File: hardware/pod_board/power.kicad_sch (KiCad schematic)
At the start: 11 parts, among them J2 12 V ACC in

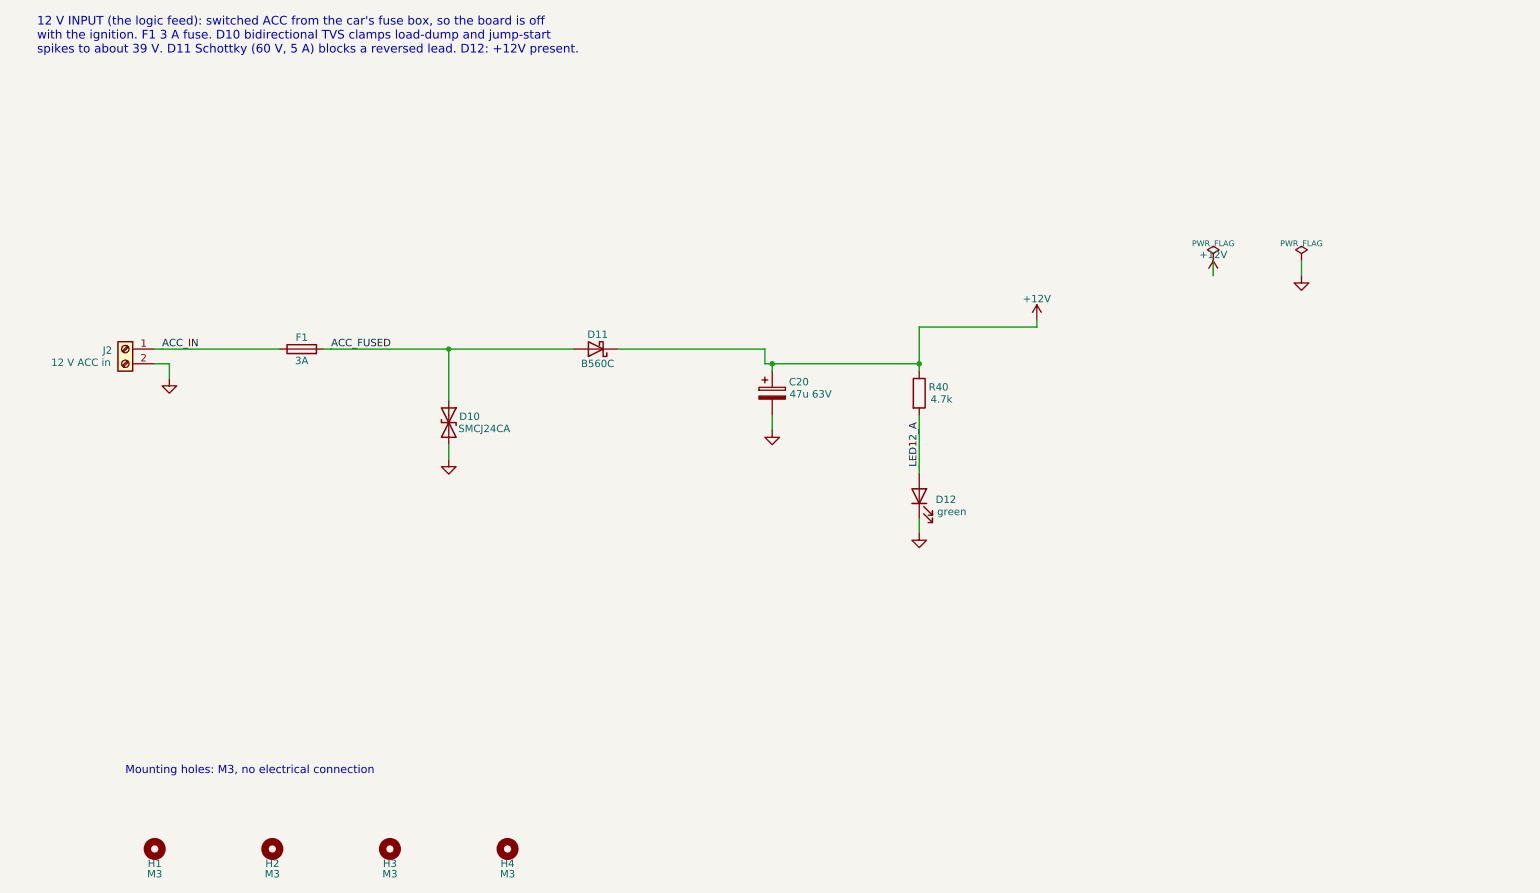
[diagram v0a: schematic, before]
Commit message: Pod board schematic redrawn as wired sheets; duplicate references fixed
pod_board_drawing.py draws six sheets around an MCU sheet under a block
diagram; check.sh now compares both boards' drawn and label-only netlists.
kisheet.py: stacked pins, PWR_FLAGs on signal nets, column hints for
crossing-free fan-ins, nets drawn in pieces joined by name, and visible
rail names on power symbols.

R31-R33 were used twice on the pod board, which KiCad's ERC does not
report; the netlist merged each pair. Cable parts now start at R40/C40,
generate.py rejects duplicate references and check_nets.py fails on a pin
in two nets. check_nets.py also drops the sheet path from net names.
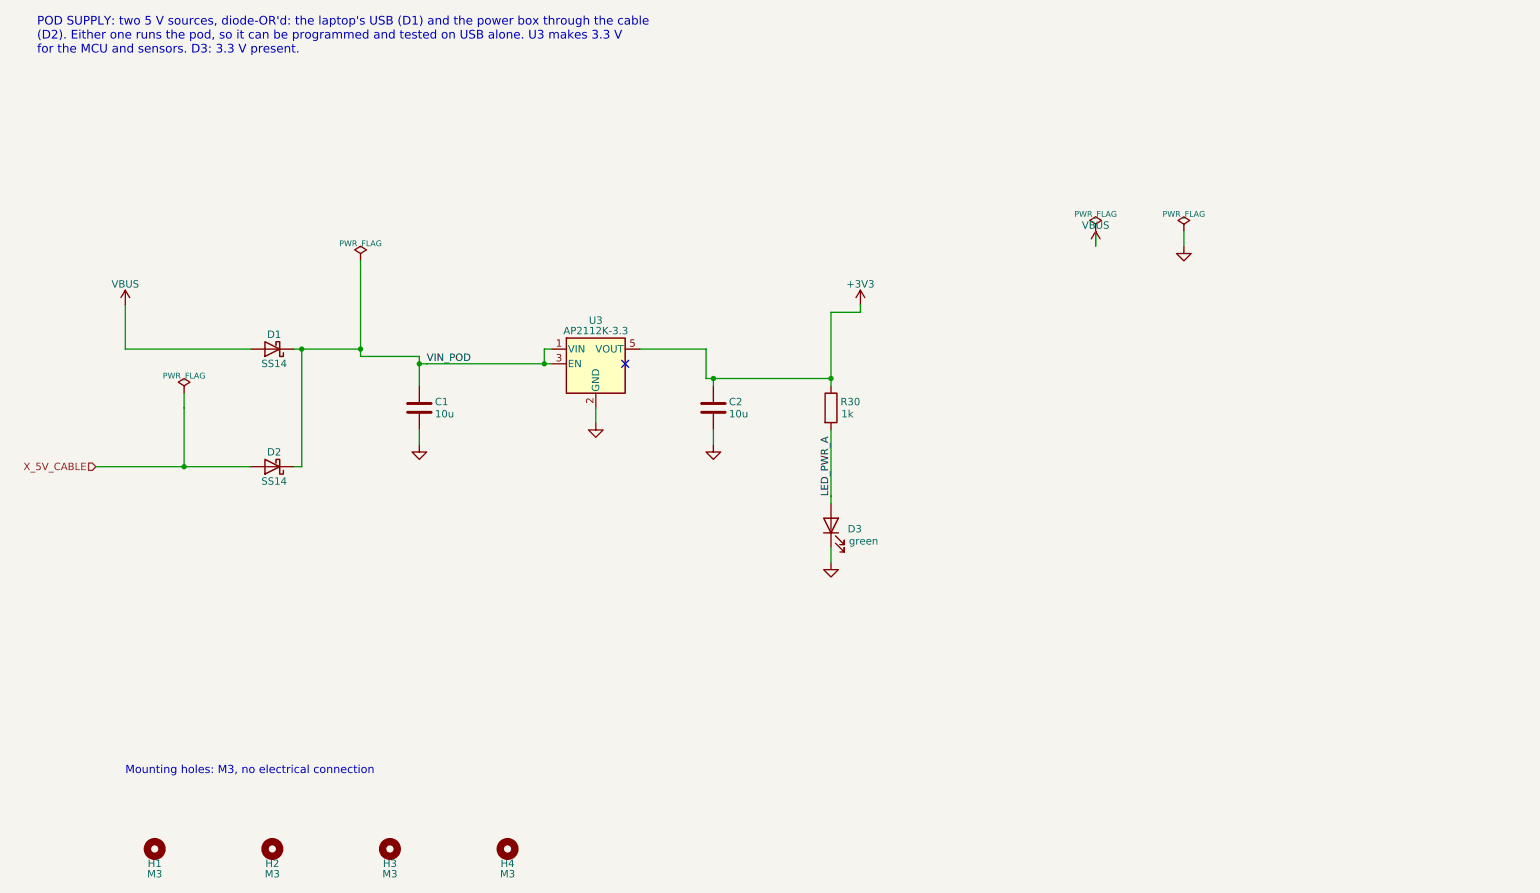
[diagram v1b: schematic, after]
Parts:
- removed C20: 47u 63V, Capacitor_THT:CP_Radial_D8.0mm_P3.50mm, symbol Device:C_Polarized
- removed D10: SMCJ24CA, Diode_SMD:D_SMC, symbol Device:D_TVS
- removed D11: B560C, Diode_SMD:D_SMC, symbol Device:D_Schottky
- removed D12: green, LED_SMD:LED_0805_2012Metric, symbol Device:LED
- removed F1: 3A, Fuse:Fuseholder_Blade_Mini_Keystone_3568, symbol Device:Fuse
- removed J2: 12 V ACC in, TerminalBlock_Phoenix:TerminalBlock_Phoenix_MKDS-1,5-2-5.08_1x02_P5.08mm_Horizontal, symbol Connector:Screw_Terminal_01x02
- removed R40: 4.7k, Resistor_SMD:R_0805_2012Metric, symbol Device:R
- added C1, C2: 10u, Capacitor_SMD:C_1206_3216Metric, symbol Device:C
- added D1, D2: SS14, Diode_SMD:D_SMA, symbol Device:D_Schottky
- added D3: green, LED_SMD:LED_0805_2012Metric, symbol Device:LED
- added R30: 1k, Resistor_SMD:R_0805_2012Metric, symbol Device:R
- added U3: AP2112K-3.3, Package_TO_SOT_SMD:SOT-23-5, symbol Regulator_Linear:AP2112K-3.3
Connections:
- net GND: now also C1.2, C2.2, D3.1 (K), U3.2 (GND)
- new net +3V3: C2.1, R30.1, U3.5 (VOUT)
- new net LED_PWR_A: D3.2 (A), R30.2
- new net VBUS: D1.2 (A)
- new net VIN_POD: C1.1, D1.1 (K), D2.1 (K), U3.1 (VIN), U3.3 (EN)
- new net X_5V_CABLE: D2.2 (A)
- no-connect marks 0 -> 1
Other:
- note added: "POD SUPPLY: two 5 V sources, diode-OR'd: the laptop's USB (D1) and the power box through the cable (D2). Either one runs the pod, so it can be programmed and tested on USB alone. U3 makes 3.3 V for the MCU and sensors. D3: 3.3 V present."
- note removed: "12 V INPUT (the logic feed): switched ACC from the car's fuse box, so the board is off with the ignition. F1 3 A fuse. D10 bidirectional TVS clamps load-dump and jump-start spikes to about 39 V. D11 Schottky (60 V, 5 A) blocks a reversed lead. D12: +12V present."
- title: 12 V input and protection -> Pod supply: USB or cable 5 V, 3.3 V regulator

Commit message: PCBs routed, labelled and ready to order: Rev 1 fabrication files and buy list
Both boards placed, routed and finished by script (hardware/gen): layout.sh places
(placement.py, with silkscreen names for every terminal, port, header and button),
route.sh routes with Freerouting inside rule areas and net classes from the layout
guide and keeps a board only with 0 DRC errors, 0 unconnected and exact schematic
parity, routespec.sh checks what the DRC cannot (planes, crystal, converter loop,
IPC-2221 widths), finish.sh adds the bottom-silkscreen identification and writes
the fabrication files (gerbers, drill, BOM, positions) only when the DRC passes.

- Pod 70 x 53 mm, 4 layers: In1 solid GND, In2 +3V3, 530 teardrops; no DRC warnings.
- Power 95 x 66 mm, 2 layers, 2 oz: 10 A rail as a zone, converter re-placed (switch
  node 16 mm, feedback 7 mm, no vias; was 78 mm and 40 mm), 328 teardrops.
- Screw terminals turned to open outward; RESET/BOOT side-push on the pod's left
  edge; USB-C footprint with a 3D model (GCT USB4105).
- Pod J2 now the Adafruit 4754's JP1 row pin for pin (the old order shorted its
  3.3 V output to ground); IMU reset on a new J8; HC-05 header fed 5 V.
- Buy list per footprint and module connections in bill-of-materials.md section 10.
- LAYOUT_GUIDE rewritten as how the boards were routed and how to review them;
  decisions, progress log and BUILD_GUIDE updated; power box follows the wider board.
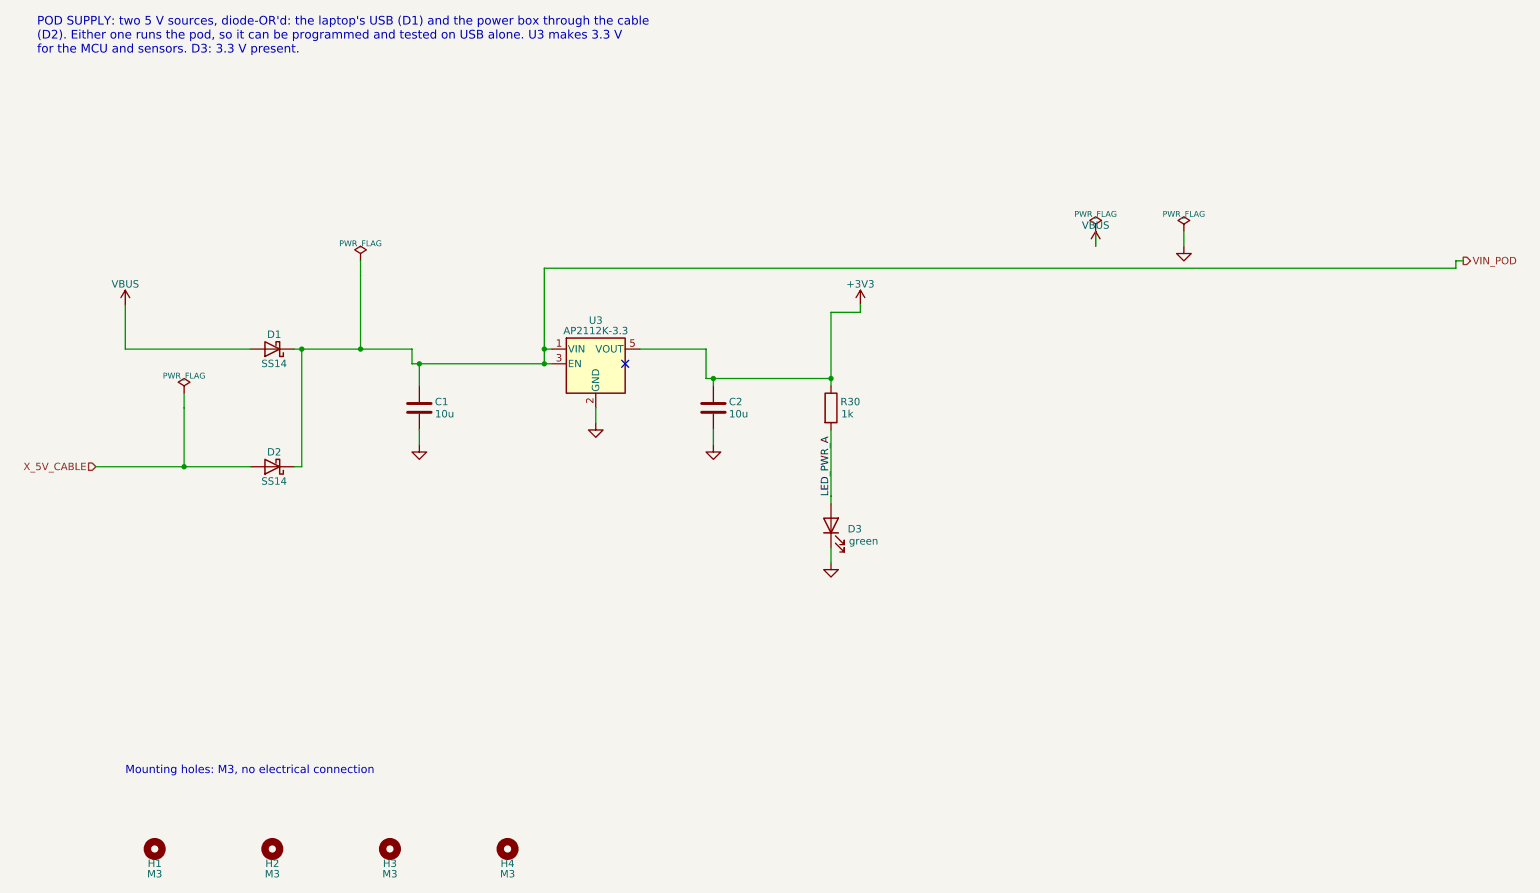
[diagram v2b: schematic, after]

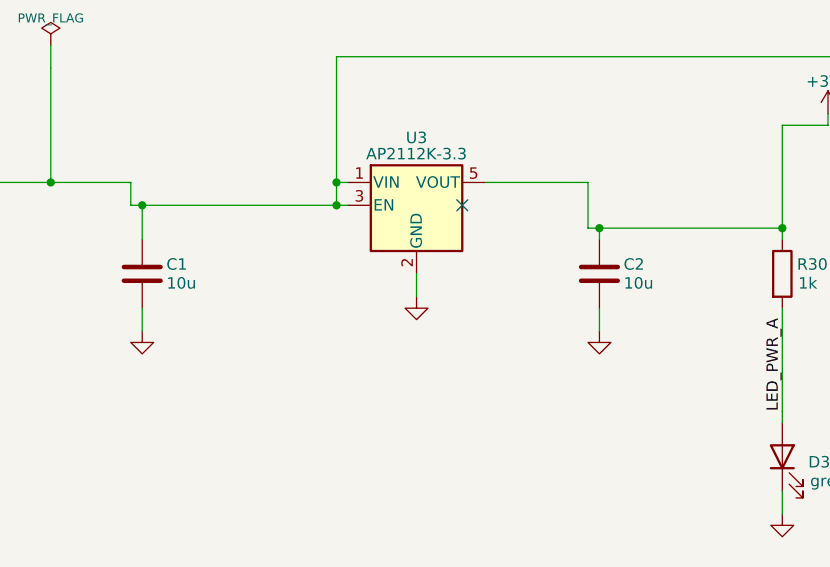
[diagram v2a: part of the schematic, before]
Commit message: Enclosures, brake-light and pod-supply simulations, R63/C1/C2 values, report drafts
Enclosures (hardware/enclosures/): the E-stop housing (yellow ASA box for the 22 mm
mushroom, M16 gland, base to a dash panel), the windscreen pod (rear cover, front shell
whose carrier wall holds board and camera, black front plate with hood, cradle with a
+-8 deg pitch lock on a rail, glass plate template) and the gesture puck (APDS-9960
module under an open window, VHB base). Typical part dimensions are marked VERIFY.
Every STL is a manifold solid.

Simulations: run_brake.sh (PC817 input through the cable to PB5: thresholds with the
weakest and strongest optocoupler, reversed wiring, jump-start, load dump, timing) and
run_pod_supply.sh (cable +5 V and USB diode-OR into the AP2112K: worst cable, lowest
USB, cable pulled while running, USB inrush, back-feed). Both ALL PASS.

Adopted from them, value changes only (copper and teardrops untouched, fab files
regenerated, DRC 0/0, parity exact): power board R63 2.2k -> 4.7k (237 mW in a 24 V
jump-start, beyond the 0805's 125 mW; now 111 mW) and pod C1/C2 10u -> 1u/4.7u (USB
attach inrush 88 uC against USB 2.0's 50 uC; now 28 uC). Order from this commit: the
pcb-rev1.1 tag predates these two changes.

Report: docs/report/final/ drafts Part 16.1 sections 2-6 and 11 from the design as
built, with [RESULT]/[FIGURE]/[CHECK] slots where tests or decisions are pending.
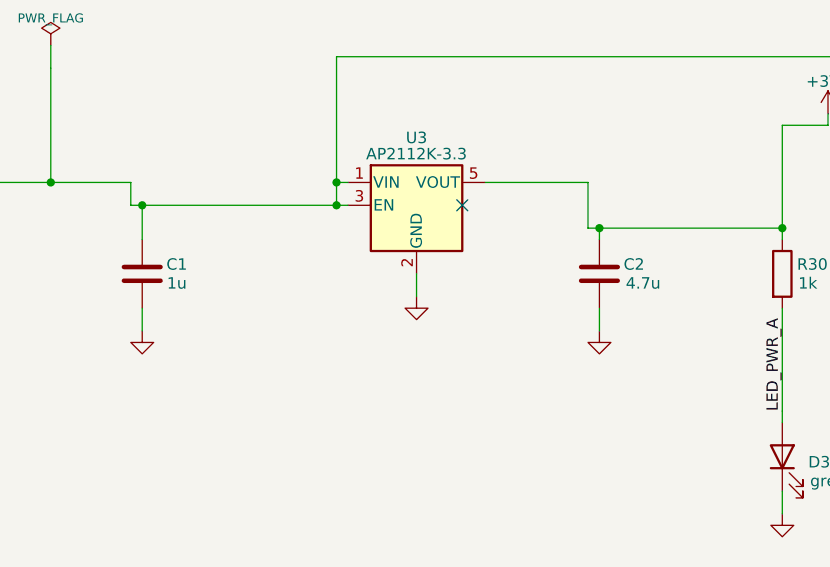
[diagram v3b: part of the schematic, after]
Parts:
- C1: value 10u -> 1u
- C2: value 10u -> 4.7u
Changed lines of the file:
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@@
 			)
 		)
-		(property "Value" "10u"
-			(at 90.716 87.41 0)
+		(property "Value" "1u"
+			(at 90.208 87.41 0)
 			(effects
 				(font
@@
 			)
 		)
-		(property "Description" ""
+		(property "Description" "1 uF, not more: USB attach inrush (hardware/sim/run_pod_supply.sh)"
 			(at 86.36 86.36 0)
 			(hide yes)
@@
 			)
 		)
-		(property "Value" "10u"
-			(at 141.516 87.41 0)
+		(property "Value" "4.7u"
+			(at 142.024 87.41 0)
 			(effects
 				(font
@@
 			)
 		)
-		(property "Description" ""
+		(property "Description" "4.7 uF, not more: USB attach inrush (hardware/sim/run_pod_supply.sh)"
 			(at 137.16 86.36 0)
 			(hide yes)
